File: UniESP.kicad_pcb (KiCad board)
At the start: 2 copper layers, 53.4 x 78.5 mm, 58 parts, among them J1 Power Conn, J2 12V Input, J3 RTC conn, J4 Extra conn, J5 Motor2_Output, J6 M2_out, J7 Motor1_Output, J8 M1_out, U1 TPS5430DDA, U2 ESP32-DevKitV1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

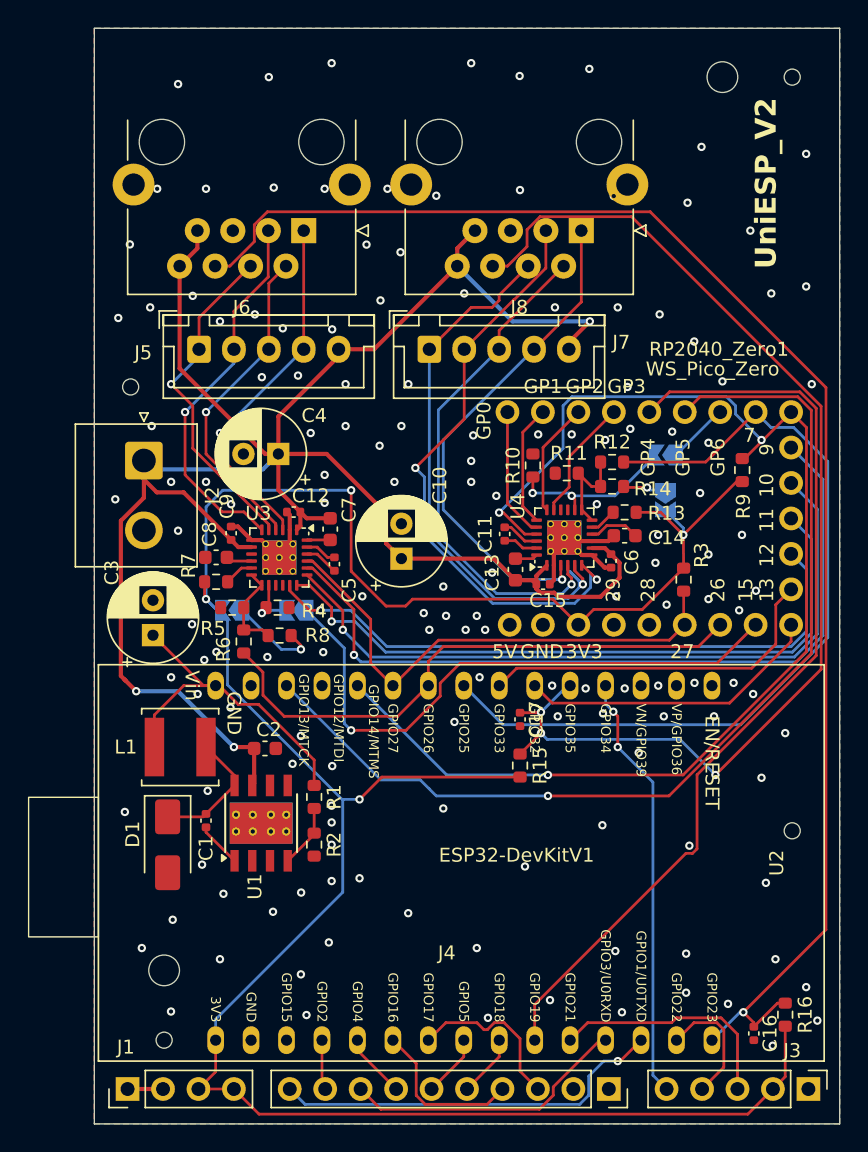
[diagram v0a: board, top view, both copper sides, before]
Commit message: Added PEC filtering
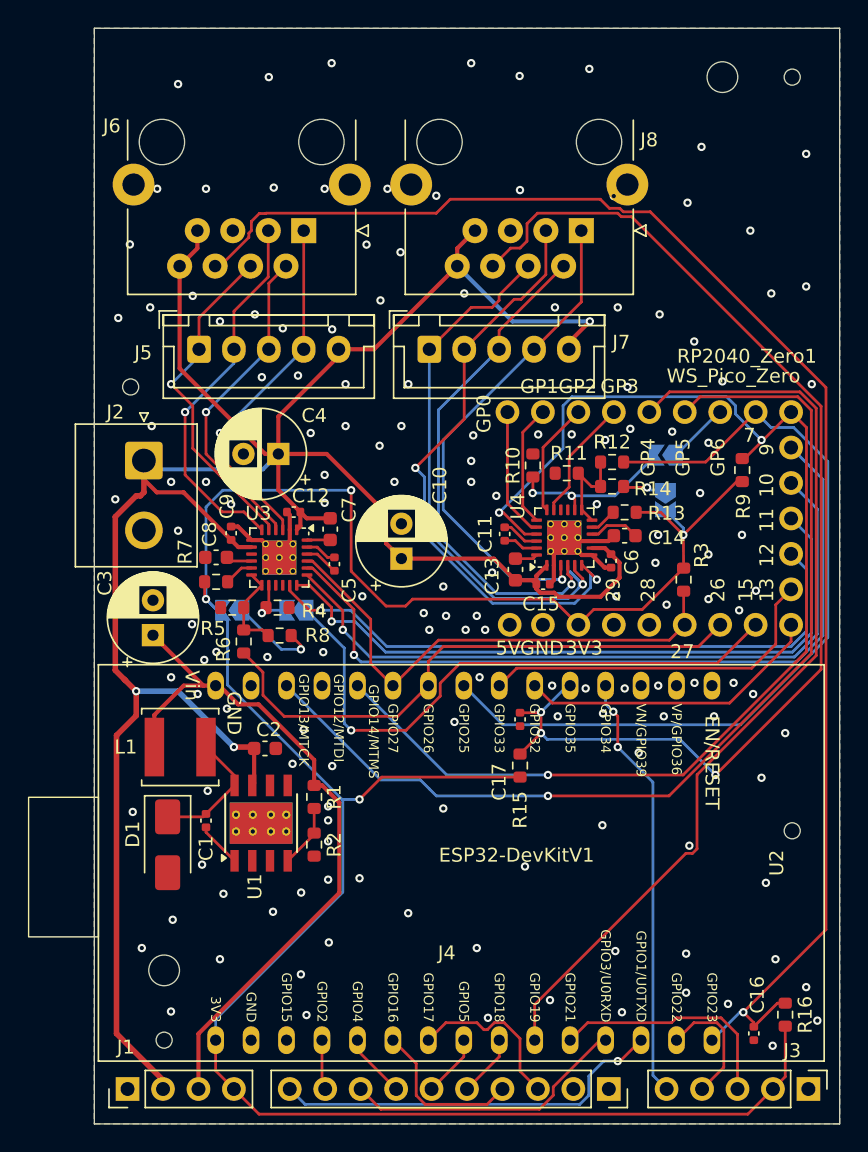
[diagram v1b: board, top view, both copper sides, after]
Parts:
- RP2040_Zero1: footprint WaveShare_pico:WS_Pico_Zero_header -> Custom:WS_Pico_Zero_header
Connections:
- J1 pad 2: GND -> +12V
- J1 pad 3: +3V3 -> +5V
- J4 pad 1: unconnected-(J4-Pin_1-Pad1) -> GND
- J4 pad 2: unconnected-(J4-Pin_2-Pad2) -> GND
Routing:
- net +12V: track 154.3 -> 185.1 mm
- net +5V: track 24.6 -> 51.7 mm
- net GND: track 16.3 -> 13.7 mm
- net +3V3: track 172.4 -> 169.9 mm
- net PEC2: track 105.9 -> 106.5 mm
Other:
- board text added: "1"
- board text added: "12V"
- board text added: "16"
- board text added: "17"
- board text added: "18"
- board text added: "2"
- board text added: "3"
- board text added: "3V3"
- board text added: "4"
- board text added: "5"
- board text added: "5V"
- board text added: "GND"
- board text added: "GPIO"
- board text added: "UniESP_V2 Nicolas Bourlet 2025"
- board text removed: "UniESP_V2"
